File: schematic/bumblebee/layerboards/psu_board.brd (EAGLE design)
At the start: 85 x 100 mm, 49 parts, among them P1 B3B-EH-A, Q1 IRF9530, Q10 IRF9530, Q2 IRF9530, Q3 IRF9530, Q5 IRF9530, Q7 IRF9530, T1 2N7002E, T2 2N7002E, T3 2N7002E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

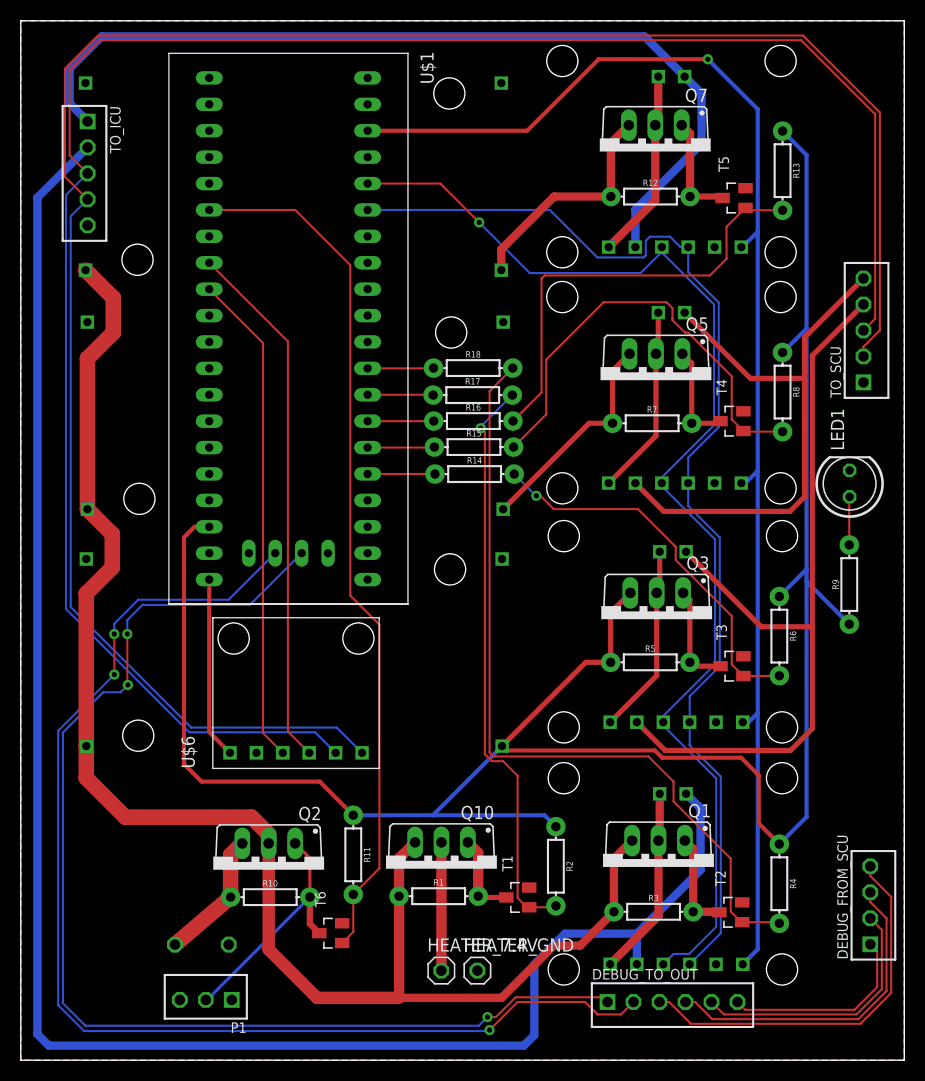
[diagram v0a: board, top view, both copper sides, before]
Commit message: Исправил библиотеку Осталось исправить внешнюю плату и сделать плату под антенну GPS
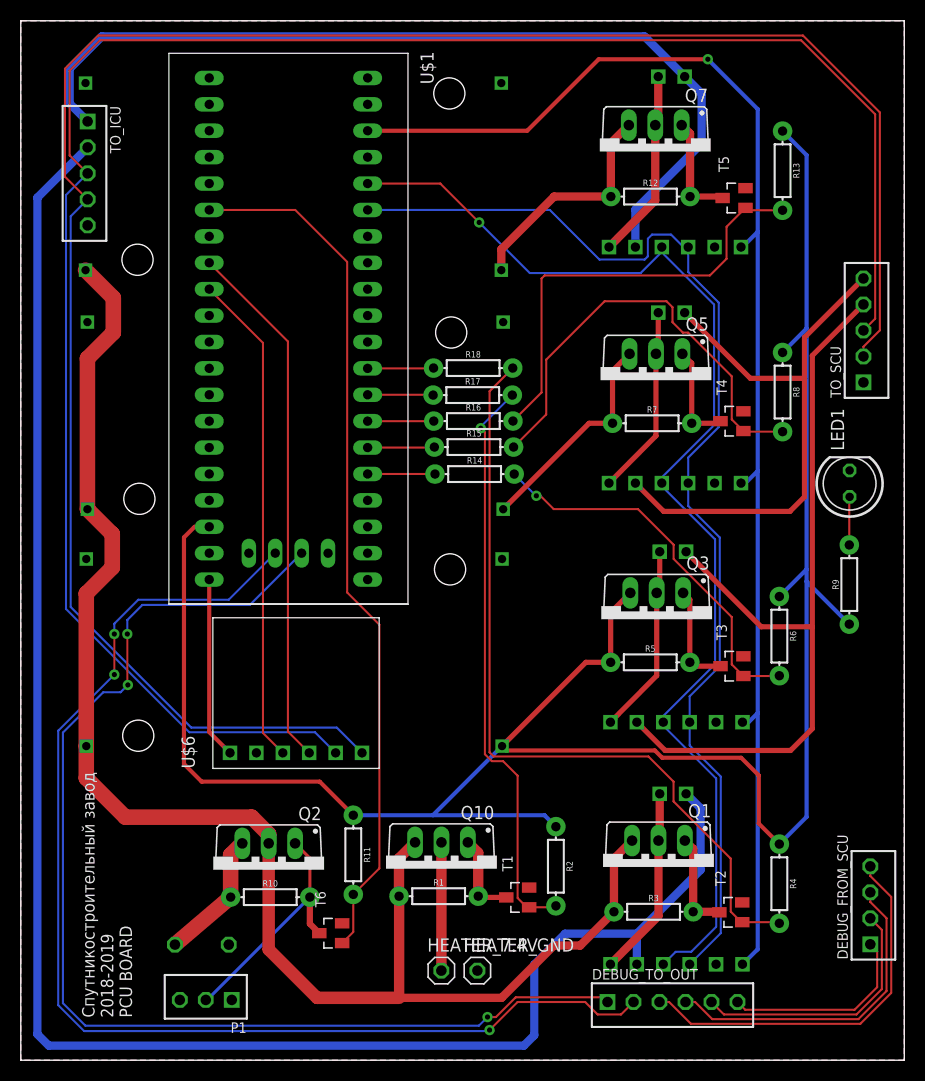
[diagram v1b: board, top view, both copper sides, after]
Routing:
- net N$13: track 111.2 -> 111.7 mm
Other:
- board text added: "Спутникостроительный завод 2018-2019 PCU BOARD"
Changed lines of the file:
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@@
 <wire x1="85" y1="100" x2="0" y2="100" width="0" layer="20"/>
 <wire x1="0" y1="100" x2="0" y2="0" width="0" layer="20"/>
+<text x="10.7" y="4.1" size="1.2" layer="21" rot="R90">Спутникостроительный завод
+2018-2019
+PCU BOARD</text>
 </plain>
 <attributes>
@@
 <wire x1="49.6" y1="54.3" x2="49.99156875" y2="54.3" width="0.2" layer="1"/>
 <wire x1="49.99156875" y1="54.3" x2="51.27156875" y2="53.02" width="0.2" layer="1"/>
-<wire x1="63.01" y1="49.39" x2="63.01" y2="48.125025" width="0.2" layer="1"/>
-<wire x1="59.38" y1="53.02" x2="63.01" y2="49.39" width="0.2" layer="1"/>
+<wire x1="62.81" y1="49.59" x2="62.81" y2="48.225025" width="0.2" layer="1"/>
+<wire x1="59.38" y1="53.02" x2="62.81" y2="49.59" width="0.2" layer="1"/>
 <wire x1="51.27156875" y1="53.02" x2="59.38" y2="53.02" width="0.2" layer="1"/>
 <wire x1="68.4" y1="38.08" x2="69.52" y2="36.96" width="0.2" layer="1"/>
-<wire x1="63.01" y1="48.125025" x2="68.4" y2="42.735025" width="0.2" layer="1"/>
-<wire x1="68.4" y1="42.735025" x2="68.4" y2="38.08" width="0.2" layer="1"/>
+<wire x1="62.81" y1="48.225025" x2="68.4" y2="42.635025" width="0.2" layer="1"/>
+<wire x1="68.4" y1="42.635025" x2="68.4" y2="38.08" width="0.2" layer="1"/>
 </signal>
 <signal name="N$3">
@@
 <wire x1="47.41" y1="58.99" x2="50.55" y2="62.13" width="0.2" layer="1"/>
 <wire x1="50.55" y1="62.13" x2="50.55" y2="67.4" width="0.2" layer="1"/>
-<wire x1="50.55" y1="67.4" x2="56.07" y2="72.92" width="0.2" layer="1"/>
-<wire x1="62.124975" y1="72.92" x2="62.7" y2="72.344975" width="0.2" layer="1"/>
-<wire x1="56.07" y1="72.92" x2="62.124975" y2="72.92" width="0.2" layer="1"/>
-<wire x1="62.7" y1="72.344975" x2="62.7" y2="71.4" width="0.2" layer="1"/>
-<wire x1="62.7" y1="71.4" x2="62.7" y2="71.2" width="0.2" layer="1"/>
-<wire x1="62.7" y1="71.2" x2="63.9" y2="70" width="0.2" layer="1"/>
-<wire x1="63.9" y1="70" x2="64.2" y2="70" width="0.2" layer="1"/>
+<wire x1="50.55" y1="67.4" x2="56.17" y2="73.02" width="0.2" layer="1"/>
+<wire x1="62.124975" y1="73.02" x2="62.7" y2="72.444975" width="0.2" layer="1"/>
+<wire x1="56.17" y1="73.02" x2="62.124975" y2="73.02" width="0.2" layer="1"/>
+<wire x1="62.7" y1="72.444975" x2="62.7" y2="71" width="0.2" layer="1"/>
+<wire x1="62.7" y1="71" x2="63.7" y2="70" width="0.2" layer="1"/>
+<wire x1="63.7" y1="70" x2="64.2" y2="70" width="0.2" layer="1"/>
 <wire x1="64.2" y1="70" x2="68.4" y2="65.8" width="0.2" layer="1"/>
 <wire x1="68.4" y1="61.65" x2="69.52" y2="60.53" width="0.2" layer="1"/>
@@
 <wire x1="61.47" y1="45.25" x2="61.18" y2="44.96" width="0.5" layer="1"/>
 <wire x1="61.18" y1="44.96" x2="61.18" y2="37" width="0.5" layer="1"/>
-<wire x1="61.18" y1="37" x2="56.7" y2="32.52" width="0.5" layer="1"/>
+<wire x1="61.18" y1="37" x2="56.73" y2="32.52" width="0.5" layer="1"/>
 </signal>
 <signal name="N$10">
@@
 <wire x1="61.33" y1="68.18" x2="61.33" y2="71.92" width="0.5" layer="1"/>
 <wire x1="61.11" y1="67.96" x2="61.11" y2="60.07" width="0.5" layer="1"/>
-<wire x1="61.11" y1="60.07" x2="56.56" y2="55.52" width="0.5" layer="1"/>
+<wire x1="61.11" y1="60.07" x2="56.59" y2="55.52" width="0.5" layer="1"/>
 </signal>
 <signal name="N$11">
@@
 <wire x1="61.33" y1="90.25" x2="61.33" y2="94.63" width="0.8" layer="1"/>
 <wire x1="61.04" y1="89.96" x2="61.04" y2="82.71" width="0.8" layer="1"/>
-<wire x1="61.04" y1="82.71" x2="56.56" y2="78.23" width="0.8" layer="1"/>
+<wire x1="61.04" y1="82.71" x2="56.59" y2="78.23" width="0.8" layer="1"/>
 </signal>
 <signal name="CANH">
@@
 <wire x1="61.47" y1="21.25" x2="61.47" y2="25.63" width="0.8" layer="1"/>
 <wire x1="61.35" y1="21.13" x2="61.35" y2="13.88" width="0.8" layer="1"/>
-<wire x1="61.35" y1="13.88" x2="56.7" y2="9.23" width="0.8" layer="1"/>
+<wire x1="61.35" y1="13.88" x2="56.73" y2="9.23" width="0.8" layer="1"/>
 </signal>
 <signal name="5V_CCU">
@@
 <wire x1="64.21" y1="75.8264" x2="64.21" y2="78.23" width="0.2" layer="16"/>
 <wire x1="67.15" y1="72.8864" x2="64.21" y2="75.8264" width="0.2" layer="16"/>
-<wire x1="64.21" y1="78.23" x2="63.464975" y2="78.23" width="0.2" layer="16"/>
-<wire x1="63.464975" y1="78.23" x2="62.464975" y2="79.23" width="0.2" layer="16"/>
-<wire x1="60.53" y1="79.23" x2="60.13" y2="78.83" width="0.2" layer="16"/>
-<wire x1="60.13" y1="77.435025" x2="59.924975" y2="77.23" width="0.2" layer="16"/>
-<wire x1="60.13" y1="78.83" x2="60.13" y2="77.435025" width="0.2" layer="16"/>
+<wire x1="64.21" y1="78.23" x2="63.764975" y2="78.23" width="0.2" layer="16"/>
+<wire x1="63.764975" y1="78.23" x2="62.564975" y2="79.43" width="0.2" layer="16"/>
+<wire x1="60.73" y1="79.43" x2="60.33" y2="79.03" width="0.2" layer="16"/>
+<wire x1="60.33" y1="77.335025" x2="60.024975" y2="77.03" width="0.2" layer="16"/>
+<wire x1="60.33" y1="79.03" x2="60.33" y2="77.335025" width="0.2" layer="16"/>
 <wire x1="50.9" y1="81.8" x2="33.37" y2="81.8" width="0.2" layer="16"/>
-<wire x1="62.464975" y1="79.23" x2="60.53" y2="79.23" width="0.2" layer="16"/>
-<wire x1="59.924975" y1="77.23" x2="55.47" y2="77.23" width="0.2" layer="16"/>
-<wire x1="55.47" y1="77.23" x2="50.9" y2="81.8" width="0.2" layer="16"/>
+<wire x1="62.564975" y1="79.43" x2="60.73" y2="79.43" width="0.2" layer="16"/>
+<wire x1="60.024975" y1="77.03" x2="55.67" y2="77.03" width="0.2" layer="16"/>
+<wire x1="55.67" y1="77.03" x2="50.9" y2="81.8" width="0.2" layer="16"/>
 </signal>
 <signal name="N$12">
@@
 <contactref element="U$8" pad="SDA"/>
 <contactref element="U$9" pad="SDA"/>
-<wire x1="61.81" y1="9.23" x2="62.81" y2="10.23" width="0.2" layer="16"/>
-<wire x1="62.81" y1="10.23" x2="64.3" y2="10.23" width="0.2" layer="16"/>
-<wire x1="64.3" y1="10.23" x2="66.9" y2="12.83" width="0.2" layer="16"/>
+<wire x1="61.81" y1="9.23" x2="63.01" y2="10.43" width="0.2" layer="16"/>
+<wire x1="63.01" y1="10.43" x2="64.5" y2="10.43" width="0.2" layer="16"/>
+<wire x1="64.5" y1="10.43" x2="66.9" y2="12.83" width="0.2" layer="16"/>
 <wire x1="66.9" y1="12.83" x2="66.9" y2="27.1" width="0.2" layer="16"/>
 <wire x1="66.9" y1="27.1" x2="61.81" y2="32.19" width="0.2" layer="16"/>
@@
 <via x="66.1" y="96.3" extent="1-16" drill="0.5"/>
 <wire x1="66.1" y1="96.3" x2="70.9" y2="91.5" width="0.4" layer="16"/>
-<wire x1="70.9" y1="10.67" x2="69.46" y2="9.23" width="0.4" layer="16"/>
+<wire x1="70.9" y1="10.67" x2="69.43" y2="9.23" width="0.4" layer="16"/>
 <wire x1="70.9" y1="91.5" x2="70.9" y2="79.7" width="0.4" layer="16"/>
 <wire x1="70.9" y1="79.7" x2="70.9" y2="56.7" width="0.4" layer="16"/>
 <wire x1="70.9" y1="56.7" x2="70.9" y2="33.4" width="0.4" layer="16"/>
 <wire x1="70.9" y1="33.4" x2="70.9" y2="10.67" width="0.4" layer="16"/>
-<wire x1="69.46" y1="32.52" x2="70.02" y2="32.52" width="0.4" layer="16"/>
+<wire x1="69.43" y1="32.52" x2="70.02" y2="32.52" width="0.4" layer="16"/>
 <wire x1="70.02" y1="32.52" x2="70.9" y2="33.4" width="0.4" layer="16"/>
-<wire x1="69.32" y1="55.52" x2="69.72" y2="55.52" width="0.4" layer="16"/>
+<wire x1="69.29" y1="55.52" x2="69.72" y2="55.52" width="0.4" layer="16"/>
 <wire x1="69.72" y1="55.52" x2="70.9" y2="56.7" width="0.4" layer="16"/>
-<wire x1="69.32" y1="78.23" x2="69.43" y2="78.23" width="0.4" layer="16"/>
+<wire x1="69.29" y1="78.23" x2="69.43" y2="78.23" width="0.4" layer="16"/>
 <wire x1="69.43" y1="78.23" x2="70.9" y2="79.7" width="0.4" layer="16"/>
 <contactref element="U$6" pad="3V3"/>
@@
 <wire x1="31.99" y1="12.34" x2="31.99" y2="15.95" width="0.2" layer="1"/>
 <wire x1="18.13" y1="81.8" x2="26.4" y2="81.8" width="0.2" layer="1"/>
-<wire x1="31.7" y1="76.5" x2="31.7" y2="44.7" width="0.2" layer="1"/>
-<wire x1="31.7" y1="44.7" x2="34.5" y2="41.9" width="0.2" layer="1"/>
+<wire x1="31.4" y1="76.8" x2="31.4" y2="45" width="0.2" layer="1"/>
+<wire x1="31.4" y1="45" x2="34.5" y2="41.9" width="0.2" layer="1"/>
 <wire x1="34.5" y1="18.46" x2="31.99" y2="15.95" width="0.2" layer="1"/>
-<wire x1="26.4" y1="81.8" x2="31.7" y2="76.5" width="0.2" layer="1"/>
+<wire x1="26.4" y1="81.8" x2="31.4" y2="76.8" width="0.2" layer="1"/>
 <wire x1="34.5" y1="41.9" x2="34.5" y2="18.46" width="0.2" layer="1"/>
 </signal>
@@
 </drawing>
 <compatibility>
+<note version="6.3" minversion="6.2.2" severity="warning">
+Since Version 6.2.2 text objects can contain more than one line,
+which will not be processed correctly with this version.
+</note>
 <note version="8.2" severity="warning">
 Since Version 8.2, EAGLE supports online libraries. The ids
